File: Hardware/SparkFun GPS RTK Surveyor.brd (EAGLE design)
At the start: 69.1 x 110.1 mm, 178 parts, among them J16 microSD, J3 USB-C, J4 Qwiic Right Angle, J6 Start Base, J7 Power Switch, Q2 MBT3904DW1T1, U1 MCP73831, U2 3.3V, U3 U-BLOX_ZED-F9P, U4 3.3V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

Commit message: Change resistor values on LEDs to try to balance brightness.
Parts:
- J3: value USB-C -> ESP32 USB
- J5: value (none) -> u-blox USB
- R1: value 1k -> 4.7k
- R11, R24, R25, R26: value 330 -> 20
- R6, R8: value 330 -> 1k
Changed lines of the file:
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@@
 <layer number="47" name="Measures" color="7" fill="1" visible="no" active="yes"/>
 <layer number="48" name="Document" color="7" fill="1" visible="no" active="yes"/>
-<layer number="49" name="Reference" color="7" fill="1" visible="yes" active="yes"/>
+<layer number="49" name="Reference" color="7" fill="1" visible="no" active="yes"/>
 <layer number="50" name="dxf" color="7" fill="1" visible="no" active="yes"/>
 <layer number="51" name="tDocu" color="6" fill="1" visible="yes" active="yes"/>
@@
 <attribute name="VALUE" x="30.988" y="53.34" size="0.6096" layer="27" font="vector" ratio="20" align="top-center"/>
 </element>
-<element name="R11" library="SparkFun-Resistors" package="0603" value="330" x="30.988" y="55.245" smashed="yes">
+<element name="R11" library="SparkFun-Resistors" package="0603" value="20" x="30.988" y="55.245" smashed="yes">
 <attribute name="NAME" x="30.988" y="56.007" size="0.6096" layer="25" font="vector" ratio="20" align="bottom-center"/>
-<attribute name="PROD_ID" value="RES-00818" x="30.988" y="55.245" size="1.778" layer="27" font="vector" ratio="15" display="off"/>
-<attribute name="VALUE" value="330" x="33.02" y="54.991" size="0.6096" layer="27" font="vector" ratio="20" rot="R180" align="top-center"/>
+<attribute name="PROD_ID" value="RES-07862" x="30.988" y="55.245" size="1.778" layer="27" font="vector" ratio="15" display="off"/>
+<attribute name="VALUE" value="20" x="33.02" y="54.991" size="0.6096" layer="27" font="vector" ratio="20" rot="R180" align="top-center"/>
 </element>
 <element name="JP71" library="SparkFun-Aesthetics" package="FIDUCIAL-MICRO" value="FIDUCIALUFIDUCIAL" x="54.61" y="4.35" smashed="yes" rot="MR0"/>
@@
 <attribute name="VALUE" x="21.717" y="11.033" size="0.6096" layer="27" font="vector" ratio="20" align="top-center"/>
 </element>
-<element name="J5" library="SparkFun-Connectors" package="USB-C-16P-2LAYER-PADS" value="" x="25.4" y="6.207" smashed="yes">
+<element name="J5" library="SparkFun-Connectors" package="USB-C-16P-2LAYER-PADS" value="u-blox USB" x="25.4" y="6.207" smashed="yes">
 <attribute name="NAME" x="25.4" y="-3.953" size="0.762" layer="25" align="center"/>
 <attribute name="PROD_ID" value="CONN-14122" x="25.4" y="6.207" size="1.778" layer="27" display="off"/>
@@
 <element name="U$43" library="output" package="SERIAL20" value="" x="-2.54" y="0.143" smashed="yes" rot="R90"/>
 <element name="U$29" library="output" package="SERIAL10" value="" x="43.307" y="-0.111" smashed="yes" rot="R90"/>
-<element name="R24" library="SparkFun-Resistors" package="0603" value="330" x="19.812" y="62.865" smashed="yes" rot="R180">
+<element name="R24" library="SparkFun-Resistors" package="0603" value="20" x="19.812" y="62.865" smashed="yes" rot="R180">
 <attribute name="NAME" x="19.812" y="62.103" size="0.6096" layer="25" font="vector" ratio="20" rot="R180" align="bottom-center"/>
-<attribute name="PROD_ID" value="RES-00818" x="19.812" y="62.865" size="1.778" layer="27" font="vector" ratio="15" rot="R180" display="off"/>
-<attribute name="VALUE" value="330" x="19.812" y="63.627" size="0.6096" layer="27" font="vector" ratio="20" rot="R180" align="top-center"/>
+<attribute name="PROD_ID" value="RES-07862" x="19.812" y="62.865" size="1.778" layer="27" font="vector" ratio="15" rot="R180" display="off"/>
+<attribute name="VALUE" value="20" x="19.812" y="63.627" size="0.6096" layer="27" font="vector" ratio="20" rot="R180" align="top-center"/>
 </element>
 <element name="D8" library="SparkFun-LED" package="LED-0603" value="GREEN" x="19.812" y="61.595" smashed="yes">
@@
 <attribute name="VALUE" value="GREEN" x="19.812" y="60.96" size="0.6096" layer="27" font="vector" ratio="20" align="top-center"/>
 </element>
-<element name="R25" library="SparkFun-Resistors" package="0603" value="330" x="19.812" y="55.245" smashed="yes" rot="R180">
+<element name="R25" library="SparkFun-Resistors" package="0603" value="20" x="19.812" y="55.245" smashed="yes" rot="R180">
 <attribute name="NAME" x="19.812" y="54.483" size="0.6096" layer="25" font="vector" ratio="20" rot="R180" align="bottom-center"/>
-<attribute name="PROD_ID" value="RES-00818" x="19.812" y="55.245" size="1.778" layer="27" font="vector" ratio="15" rot="R180" display="off"/>
-<attribute name="VALUE" value="330" x="19.812" y="56.007" size="0.6096" layer="27" font="vector" ratio="20" rot="R180" align="top-center"/>
+<attribute name="PROD_ID" value="RES-07862" x="19.812" y="55.245" size="1.778" layer="27" font="vector" ratio="15" rot="R180" display="off"/>
+<attribute name="VALUE" value="20" x="19.812" y="56.007" size="0.6096" layer="27" font="vector" ratio="20" rot="R180" align="top-center"/>
 </element>
 <element name="D10" library="SparkFun-LED" package="LED-0603" value="GREEN" x="19.812" y="53.975" smashed="yes">
@@
 <attribute name="VALUE" value="GREEN" x="19.812" y="53.34" size="0.6096" layer="27" font="vector" ratio="20" align="top-center"/>
 </element>
-<element name="R26" library="SparkFun-Resistors" package="0603" value="330" x="19.812" y="47.625" smashed="yes" rot="R180">
+<element name="R26" library="SparkFun-Resistors" package="0603" value="20" x="19.812" y="47.625" smashed="yes" rot="R180">
 <attribute name="NAME" x="19.812" y="46.863" size="0.6096" layer="25" font="vector" ratio="20" rot="R180" align="bottom-center"/>
-<attribute name="PROD_ID" value="RES-00818" x="19.812" y="47.625" size="1.778" layer="27" font="vector" ratio="15" rot="R180" display="off"/>
-<attribute name="VALUE" value="330" x="19.812" y="48.387" size="0.6096" layer="27" font="vector" ratio="20" rot="R180" align="top-center"/>
+<attribute name="PROD_ID" value="RES-07862" x="19.812" y="47.625" size="1.778" layer="27" font="vector" ratio="15" rot="R180" display="off"/>
+<attribute name="VALUE" value="20" x="19.812" y="48.387" size="0.6096" layer="27" font="vector" ratio="20" rot="R180" align="top-center"/>
 </element>
 <element name="D11" library="SparkFun-LED" package="LED-0603" value="GREEN" x="19.812" y="46.355" smashed="yes">
@@
 <attribute name="VALUE" x="2.413" y="88.9" size="0.6096" layer="28" font="vector" ratio="20" rot="MR90" align="top-center"/>
 </element>
-<element name="J3" library="SparkFun-Connectors" package="USB-C-16P-2LAYER-PADS" value="USB-C" x="36.83" y="6.207" smashed="yes">
+<element name="J3" library="SparkFun-Connectors" package="USB-C-16P-2LAYER-PADS" value="ESP32 USB" x="36.83" y="6.207" smashed="yes">
 <attribute name="NAME" x="36.83" y="3.667" size="0.762" layer="25" align="center"/>
 <attribute name="PROD_ID" value="CONN-14122" x="31.75" y="-26.813" size="1.778" layer="27" font="vector" ratio="15" display="off"/>
@@
 <attribute name="VALUE" x="43.18" y="33.401" size="0.6096" layer="27" font="vector" ratio="20" align="top-center"/>
 </element>
-<element name="R1" library="SparkFun-Resistors" package="0603" value="1k" x="39.116" y="36.83" smashed="yes" rot="R180">
+<element name="R1" library="SparkFun-Resistors" package="0603" value="4.7k" x="39.116" y="36.83" smashed="yes" rot="R180">
 <attribute name="NAME" x="39.116" y="36.068" size="0.6096" layer="25" font="vector" ratio="20" rot="R180" align="bottom-center"/>
-<attribute name="PROD_ID" value="RES-07856" x="39.116" y="36.83" size="1.778" layer="27" font="vector" ratio="15" rot="R180" display="off"/>
-<attribute name="VALUE" x="39.116" y="37.592" size="0.6096" layer="27" font="vector" ratio="20" rot="R180" align="top-center"/>
-</element>
-<element name="R6" library="SparkFun-Resistors" package="0603" value="330" x="39.116" y="33.782" smashed="yes" rot="R180">
+<attribute name="PROD_ID" value="RES-07857" x="39.116" y="36.83" size="1.778" layer="27" font="vector" ratio="15" rot="R180" display="off"/>
+<attribute name="VALUE" value="4.7k" x="39.116" y="37.592" size="0.6096" layer="27" font="vector" ratio="20" rot="R180" align="top-center"/>
+</element>
+<element name="R6" library="SparkFun-Resistors" package="0603" value="1k" x="39.116" y="33.782" smashed="yes" rot="R180">
 <attribute name="NAME" x="39.116" y="33.02" size="0.6096" layer="25" font="vector" ratio="20" rot="R180" align="bottom-center"/>
-<attribute name="PROD_ID" value="RES-00818" x="39.116" y="33.782" size="1.778" layer="27" font="vector" ratio="15" rot="R180" display="off"/>
-<attribute name="VALUE" x="39.116" y="34.544" size="0.6096" layer="27" font="vector" ratio="20" rot="R180" align="top-center"/>
-</element>
-<element name="R8" library="SparkFun-Resistors" package="0603" value="330" x="39.116" y="35.306" smashed="yes" rot="R180">
+<attribute name="PROD_ID" value="RES-07856" x="39.116" y="33.782" size="1.778" layer="27" font="vector" ratio="15" rot="R180" display="off"/>
+<attribute name="VALUE" value="1k" x="39.116" y="34.544" size="0.6096" layer="27" font="vector" ratio="20" rot="R180" align="top-center"/>
+</element>
+<element name="R8" library="SparkFun-Resistors" package="0603" value="1k" x="39.116" y="35.306" smashed="yes" rot="R180">
 <attribute name="NAME" x="39.116" y="34.544" size="0.6096" layer="25" font="vector" ratio="20" rot="R180" align="bottom-center"/>
-<attribute name="PROD_ID" value="RES-00818" x="39.116" y="35.306" size="1.778" layer="27" font="vector" ratio="15" rot="R180" display="off"/>
-<attribute name="VALUE" x="39.116" y="36.068" size="0.6096" layer="27" font="vector" ratio="20" rot="R180" align="top-center"/>
+<attribute name="PROD_ID" value="RES-07856" x="39.116" y="35.306" size="1.778" layer="27" font="vector" ratio="15" rot="R180" display="off"/>
+<attribute name="VALUE" value="1k" x="39.116" y="36.068" size="0.6096" layer="27" font="vector" ratio="20" rot="R180" align="top-center"/>
 </element>
 <element name="U4" library="SparkFun-IC-Power" package="SOT23-5" value="3.3V" x="25.4" y="45.72" smashed="yes" rot="R90">

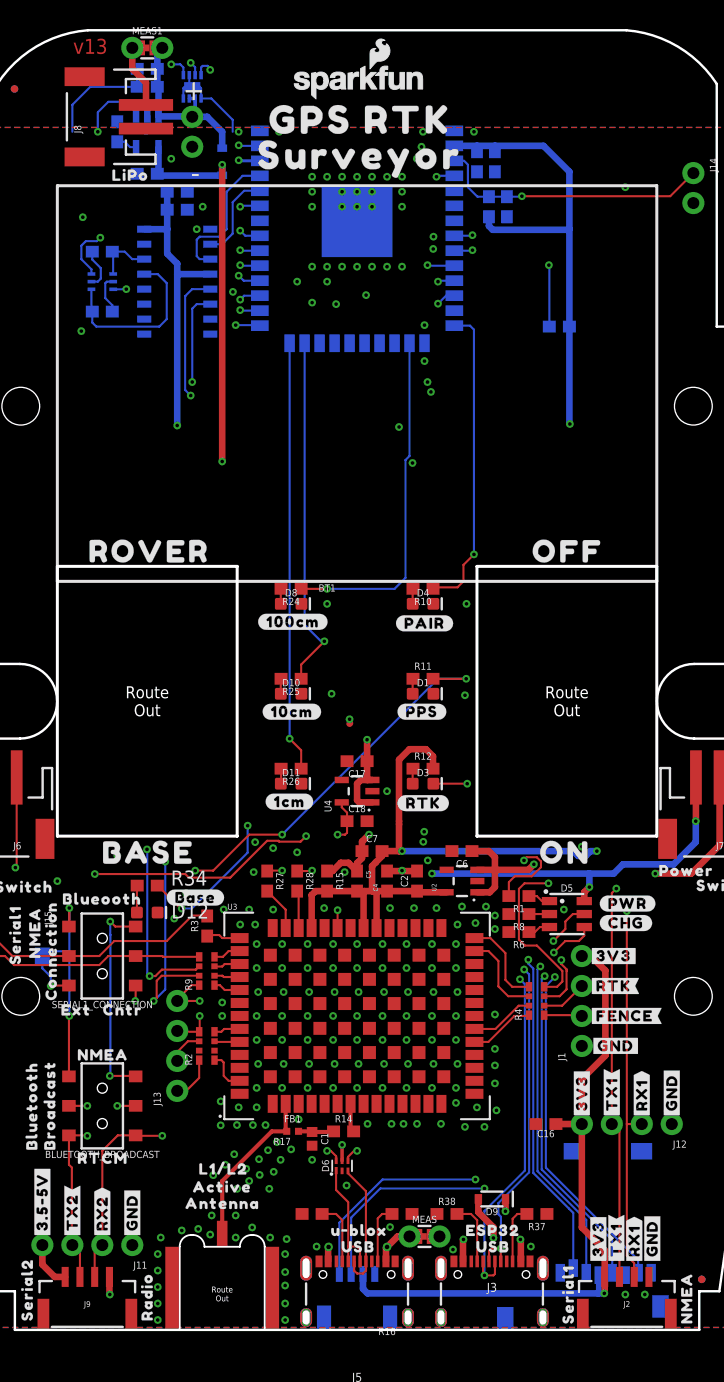
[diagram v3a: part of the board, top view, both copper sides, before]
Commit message: Add ESD protection to ESP USB. Change charge IC with 42C temp limit. Reroute ZED USB.
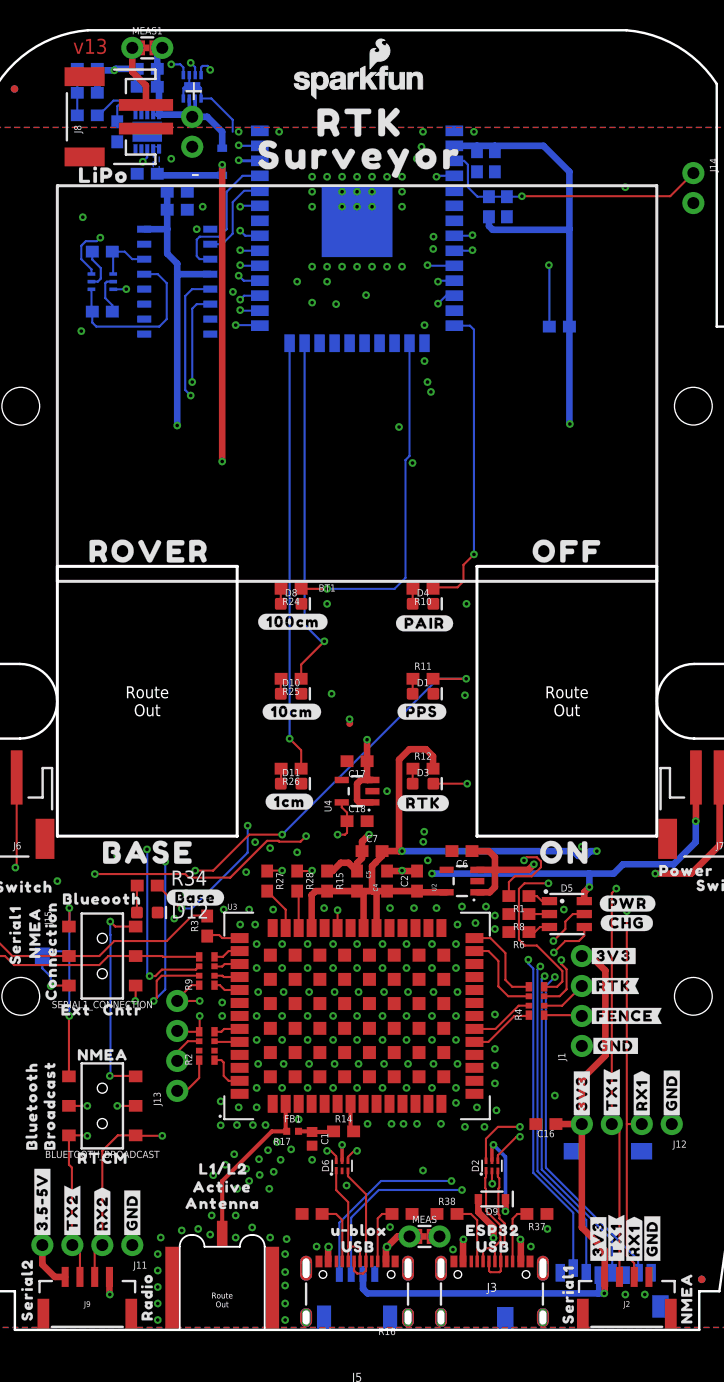
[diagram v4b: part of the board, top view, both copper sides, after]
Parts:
- removed U$70: (no value), output:GPS_RTK0
- removed U1: MCP73831, SparkFun-IC-Power:SOT23-5
- added D2: PRTR5V0U2F, SparkFun-IC-Power:SOT886
- added FRAME1: FRAME-LETTERNO_PACKAGE, SparkFun-Aesthetics:DUMMY
- added R18: 10k, SparkFun-Resistors:0603
- added R30: 150k, SparkFun-Resistors:0603
- added R5: 0, SparkFun-Resistors:0603
- added U$74: (no value), output:RTK0
- added U10: MCP73833, SparkFun-IC-Power:DFN-10
- J3: value ESP32 USB -> USB Female Type C Connector; device SparkFun-Connectors:USB-C-16P-2LAYER-PADS -> SparkFun-Connectors:USB-C-16P_4LAYER-PADS
- J5: value u-blox USB -> USB Female Type C Connector; device SparkFun-Connectors:USB-C-16P-2LAYER-PADS -> SparkFun-Connectors:USB-C-16P_4LAYER-PADS
- U$7: device output:GPS_RTK0 -> output:RTK0
- moved U$7 9.27 mm to (25.4, 53.3)
- moved U$8 2.29 mm to (48.3, 34.5)
- turned R7 to 90 degrees
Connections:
- net N$7 renamed LIPO_RAW
- new net CHG_THERM1: R18.2, R30.2, R5.2
- new net ESP_D1+: D2.3, J3.A6, J3.B6
- new net ESP_D1-: D2.1, J3.A7, J3.B7
- new net PROG1: R7.2, U10.6
- net CHG_LED: now also U10.3; no longer U1.1
- net D+1: now also D2.4; no longer J3.A6, J3.B6
- net D-1: now also D2.6; no longer J3.A7, J3.B7
- net GND: now also D2.2, R18.1, R30.1, U10.11, U10.5; no longer U1.2
- net N$5: now also R5.1, U10.8; no longer R7.2, U1.5
- net VIN: now also D2.5, U10.1, U10.2; no longer U1.4
- net V_BATT: now also U10.10, U10.9; no longer U1.3
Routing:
- net D-1: track 113.2 -> 100.9 mm, vias 4 -> 3
- net ESP_D1+: track 0.00 -> 10.8 mm
- net D+1: track 113.6 -> 103.1 mm, vias 4 -> 3
- net ESP_D1-: track 0.00 -> 10.4 mm
- net CHG_LED: track 107.9 -> 100.1 mm
- net D-: track 26.9 -> 32.3 mm
- net VIN: track 184.4 -> 189.7 mm, vias 8 -> 9
- net CHG_THERM1: track 0.00 -> 3.94 mm
- net N$5: track 1.78 -> 5.65 mm
- net PROG1: track 0.00 -> 3.65 mm
- net GND: track 34.1 -> 37.5 mm, vias 190 -> 195
- net V_BATT: track 89.5 -> 91.0 mm
- net ESP_21/SDA: track 163.3 -> 164.8 mm
- net D+: track 32.6 -> 32.1 mm, vias 3 -> 2
- added copper zone on layer 16, net VIN

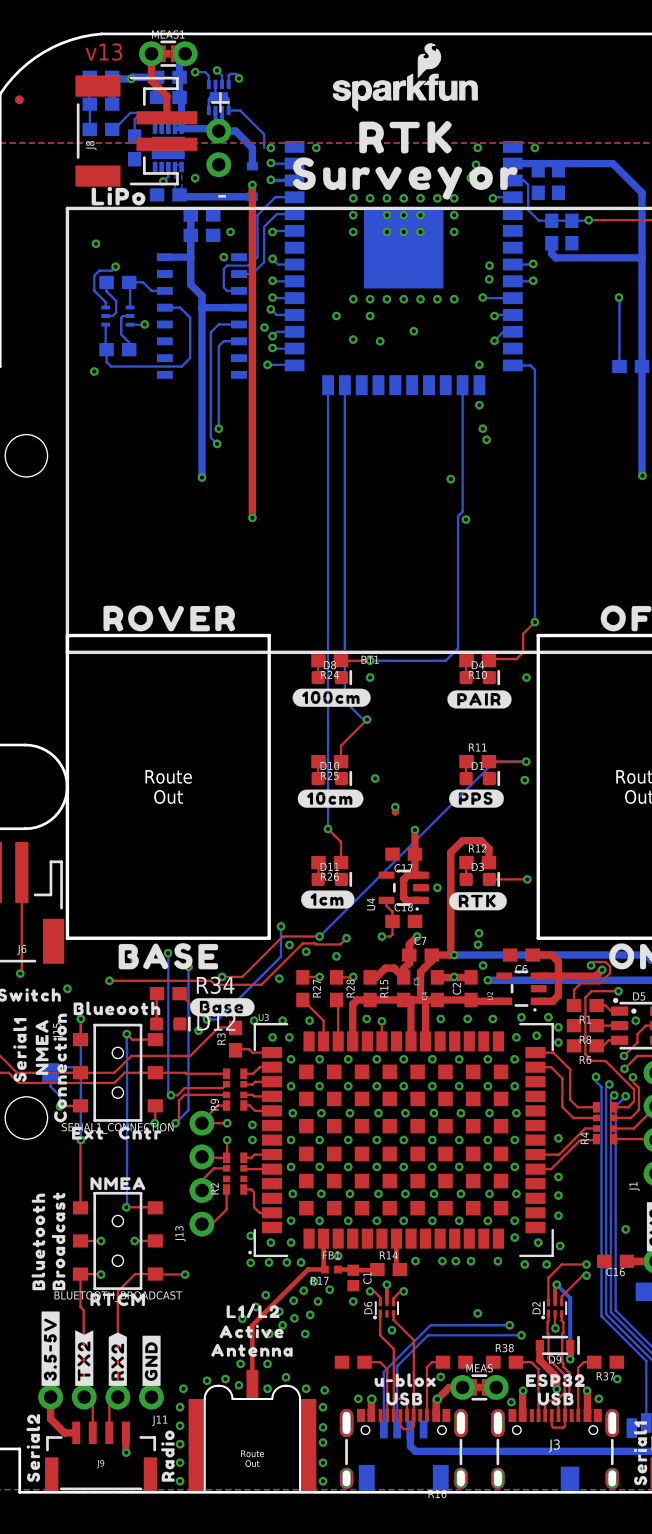
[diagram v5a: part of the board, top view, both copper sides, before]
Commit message: v1.5: Add I2C and D_SEL PTH connections.
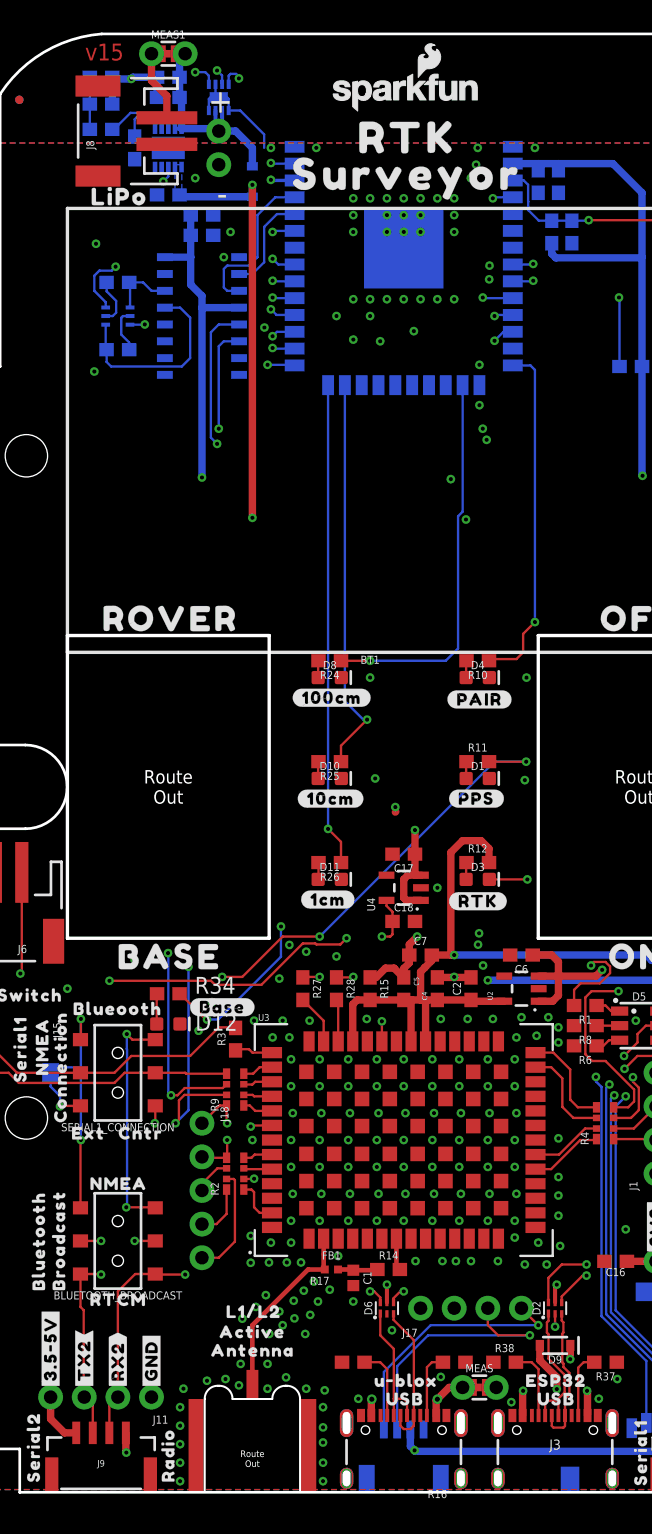
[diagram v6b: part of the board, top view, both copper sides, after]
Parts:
- removed J13: (no value), SparkFun-Connectors:1X04_NO_SILK
- added J17: Qwiic Right Angle, SparkFun-Connectors:1X04_NO_SILK
- added J18: (no value), SparkFun-Connectors:1X05_NO_SILK
- added U$70: (no value), output:#GND#2
- added U$85: (no value), output:#3V3#2
- added U$86: (no value), output:#SCL#1
- added U$87: (no value), output:#SDA#0
- added U$88: (no value), output:#D_SEL#0
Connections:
- net N$16 renamed ESP_27/ZED_!RESET!_LV
- net N$18 renamed ZED_!SAFE!_LV
- net N$22 renamed ESP_26/ZED_TX_READY_LV
- new net ZED_D_SEL: J18.5, R2.P7
- new net ZED_D_SEL_LV: R2.P2, U3.47
- net 3.3V: now also J17.2
- net ESP_21/SDA: now also J17.3
- net ESP_22/SCL: now also J17.4
- net ESP_26/ZED_TX_READY: now also J18.1; no longer J13.4
- net ESP_27/ZED_!RESET!: now also J18.2; no longer J13.3
- net GND: now also J17.1
- net ZED_!SAFE!: now also J18.3; no longer J13.2
- net ZED_PPS_STAT: now also J18.4; no longer J13.1
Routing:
- net 3.3V: track 257.6 -> 269.6 mm, vias 6 -> 7
- net ZED_D_SEL: track 0.00 -> 8.31 mm
- net ZED_D_SEL_LV: track 0.00 -> 6.99 mm, vias 0 -> 2
- net ESP_21/SDA: track 164.8 -> 169.6 mm
- net ESP_22/SCL: track 169.5 -> 171.3 mm
- net ESP_26/ZED_TX_READY: track 83.3 -> 82.7 mm
- net GND: vias 195 -> 193
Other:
- board text added: "v15"
- board text removed: "v13"
